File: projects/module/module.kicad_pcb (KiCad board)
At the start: 2 copper layers, 21 x 51 mm, 18 parts, among them J1 Conn_01x08_Pin, Y1 Crystal_GND24

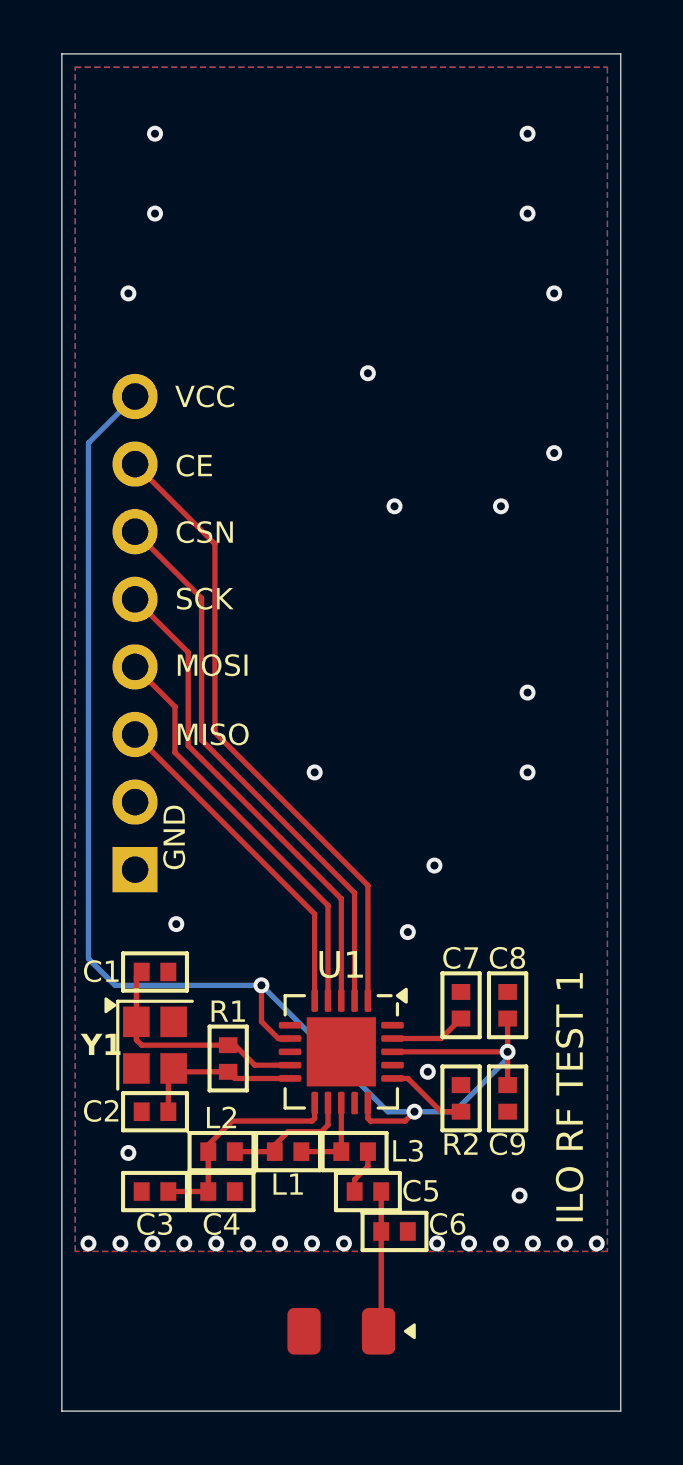
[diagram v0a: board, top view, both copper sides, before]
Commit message: Added breakout module. Added custom thin header holes. Sunk USB-C
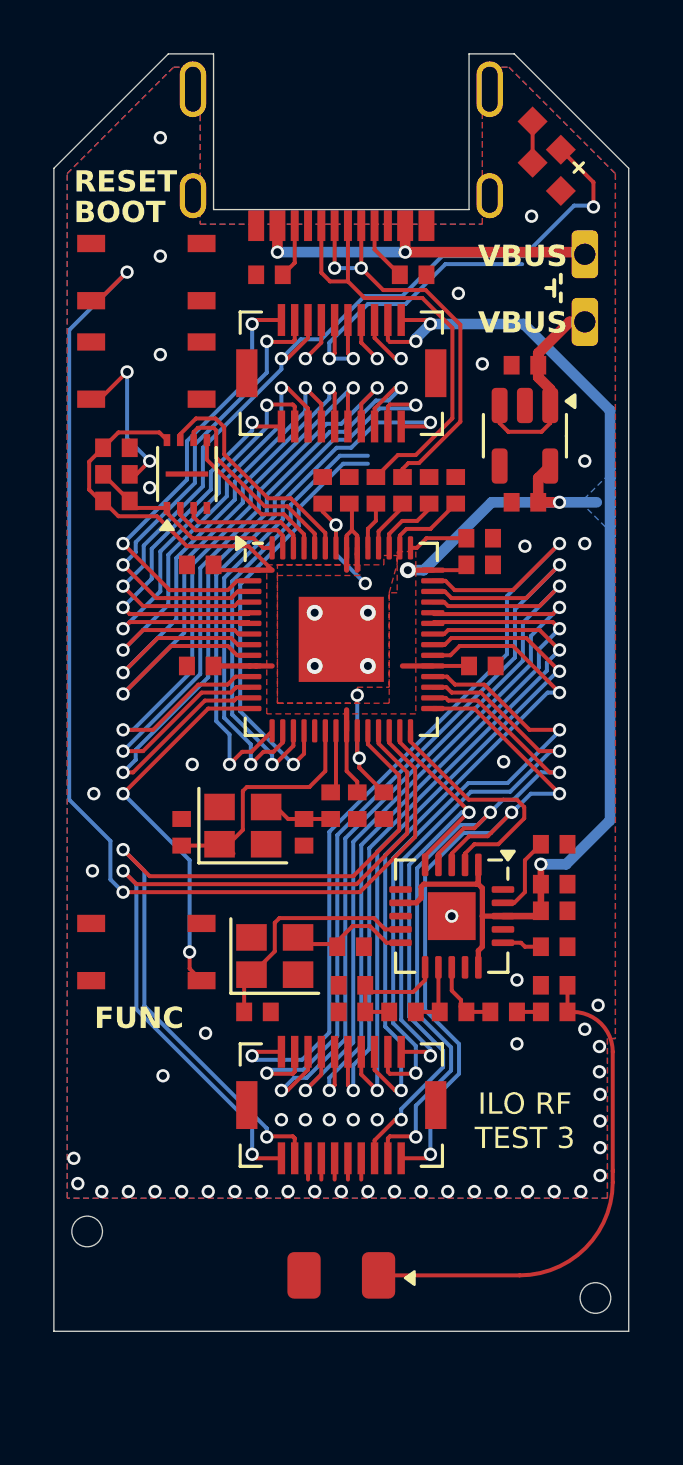
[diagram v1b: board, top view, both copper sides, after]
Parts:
- removed R1: 1M, ILO_fp:0402
- added C1: 1uF, ILO_fp:0402_compact, F.Cu at (46.9, 41.7)
- added C10: 1uF, ILO_fp:0402_compact, F.Cu at (44.3, 46.4)
- added C11: 100nF, ILO_fp:0402_compact, F.Cu at (34.7, 49.2)
- added C12: 100nF, ILO_fp:0402_compact, F.Cu at (45.3, 53.0)
- added C13: 100nF, ILO_fp:0402_compact, F.Cu at (34.7, 53.0)
- added C14: 100nF, ILO_fp:0402_compact, F.Cu at (40.6, 58.2)
- added C15: 100nF, ILO_fp:0402_compact, F.Cu at (45.2, 49.2)
- added C16: 100nF, ILO_fp:0402_compact, F.Cu at (45.2, 48.2)
- added C2: 15pF, ILO_fp:0402_compact, F.Cu at (34.0, 59.2)
- added C20: 100nF, ILO_fp:0402_compact, F.Cu at (31.6, 44.8)
- added C3: 15pF, ILO_fp:0402_compact, F.Cu at (38.6, 59.2)
- added C4: 1uF, ILO_fp:0402_compact, F.Cu at (46.9, 46.9)
- added C6: 100nF, ILO_fp:0402_compact, F.Cu at (39.3, 46.4)
- added C7: 100nF, ILO_fp:0402_compact, F.Cu at (41.6, 58.2)
- added C8: 1uF, ILO_fp:0402_compact, F.Cu at (43.3, 46.4)
- added C9: 100nF, ILO_fp:0402_compact, F.Cu at (40.3, 46.4)
- added D1: Diode, ILO_fp:0603_d, F.Cu at (47.7, 33.1)
- added J2: Conn_01x20_Pin, ILO_fp:Hirose_DF12NB, F.Cu at (40.0, 42.0)
- added J3: Conn_01x20_Pin, ILO_fp:Hirose_DF12NB, F.Cu at (40.0, 69.5)
- added R20: 1KΩ, ILO_fp:0402_compact, F.Cu at (31.6, 45.8)
- added R21: 10KΩ, ILO_fp:0402_compact, F.Cu at (31.6, 46.8)
- added R3: 27Ω, ILO_fp:0402_compact, F.Cu at (41.3, 46.4)
- added R4: 27Ω, ILO_fp:0402_compact, F.Cu at (42.3, 46.4)
- added R5: 1KΩ, ILO_fp:0402_compact, F.Cu at (39.6, 58.2)
- added R50: 5.1KΩ, ILO_fp:0402_compact, F.Cu at (42.7, 38.3)
- added R51: 5.1KΩ, ILO_fp:0402_compact, F.Cu at (37.3, 38.3)
- added R6: 20Ω, ILO_fp:0603, F.Cu at (47.7, 34.6)
- added REF**: SMT, ILO_fp:JLCPCB_SMT_hole, F.Cu at (49.5, 76.8)
- added REF**: SMT, ILO_fp:JLCPCB_SMT_hole, F.Cu at (30.4, 74.2)
- added SW1: SW_Push, ILO_fp:Alpsalpine_SKRP_compact, F.Cu at (32.7, 41.9)
- added SW2: SW_Push, ILO_fp:Alpsalpine_SKRP_compact, F.Cu at (32.7, 38.2)
- added SW3: SW_Push, ILO_fp:Alpsalpine_SKRP_compact, F.Cu at (32.7, 63.8)
- added SW4: SW_Push, ILO_fp:Header_2x_compact, F.Cu at (49.1, 37.5)
- added U2: FLASH, ILO_fp:Winbond_W25Q, F.Cu at (34.2, 45.8)
- added U4: NRF24, ILO_fp:QFN20_internal_routing, F.Cu at (44.1, 62.4)
- added U5: LDK130, Package_TO_SOT_SMD:SOT-23-5, F.Cu at (46.9, 44.4)
- added Y1: 12MHz, Crystal:Crystal_SMD_2520-4Pin_2.5x2.0mm, F.Cu at (36.3, 59.0)
- C40: renamed from C9; footprint ILO_fp:0402 -> ILO_fp:0402_compact
- C41: renamed from C8; footprint ILO_fp:0402 -> ILO_fp:0402_compact
- C42: renamed from C7; footprint ILO_fp:0402 -> ILO_fp:0402_compact
- C43: renamed from C1; footprint ILO_fp:0402 -> ILO_fp:0402_compact
- C44: renamed from C2; footprint ILO_fp:0402 -> ILO_fp:0402_compact
- C45: renamed from C3; footprint ILO_fp:0402 -> ILO_fp:0402_compact
- C46: renamed from C4; footprint ILO_fp:0402 -> ILO_fp:0402_compact
- C47: renamed from C5; footprint ILO_fp:0402 -> ILO_fp:0402_compact
- C48: renamed from C6; value 1.0pF -> 1pF; footprint ILO_fp:0402 -> ILO_fp:0402_compact
- J1: value Conn_01x08_Pin -> USB_C; footprint Connector_PinHeader_2.54mm:PinHeader_1x08_P2.54mm_Vertical -> ILO_fp:USB_C2927298
- L1, L2, L3: footprint ILO_fp:0402 -> ILO_fp:0402_compact
- R40: renamed from R2; value 22K -> 22KΩ; footprint ILO_fp:0402 -> ILO_fp:0402_compact
- U1: value ~ -> RP2040; footprint Package_DFN_QFN:QFN-20-1EP_4x4mm_P0.5mm_EP2.6x2.6mm -> Package_DFN_QFN:QFN-56-1EP_7x7mm_P0.4mm_EP3.2x3.2mm
- Y2: renamed from Y1; value Crystal_GND24 -> 16MHz
- moved U1 15.5 mm to (40.0, 52.0), turned to 0 degrees
- moved J1 11.9 mm to (40.0, 33.9), turned to 180 degrees
- moved C48 11.0 mm to (48.0, 65.0), turned to 180 degrees
- moved C45 10.0 mm to (40.4, 66.0)
- moved C47 9.72 mm to (48.0, 66.0)
- moved C44 9.62 mm to (40.4, 63.5), turned to 0 degrees
- moved C46 9.17 mm to (40.4, 65.0), turned to 180 degrees
- moved L2 8.59 mm to (42.3, 66.0)
- moved C40 8.24 mm to (48.0, 61.2), turned to 0 degrees
- moved L1 8.12 mm to (44.2, 66.0)
- moved L3 7.68 mm to (46.1, 66.0)
- moved C42 6.99 mm to (48.0, 59.7), turned to 0 degrees
- moved R40 6.69 mm to (48.0, 63.5), turned to 180 degrees
- moved Y2 5.61 mm to (37.5, 63.9), turned to 0 degrees
- moved C43 4.13 mm to (36.9, 66.0)
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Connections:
- C40 pad 1: VCC -> +3V3
- C41 pad 1: VCC -> +3V3
- C42 pad 1: GND -> Net-(U4-DVDD)
- C42 pad 2: Net-(U1-DVDD) -> GND
- C43 pad 1: Net-(U1-XC2) -> Net-(U4-XC2)
- C44 pad 1: Net-(U1-XC1) -> Net-(U4-XC1)
- C45 pad 1: Net-(U1-VDDPA) -> Net-(U4-VDDPA)
- C46 pad 1: Net-(U1-VDDPA) -> Net-(U4-VDDPA)
- L1 pad 1: Net-(U1-ANT2) -> Net-(U4-ANT2)
- L1 pad 2: Net-(U1-ANT1) -> Net-(U4-ANT1)
- L2 pad 1: Net-(U1-ANT1) -> Net-(U4-ANT1)
- L2 pad 2: Net-(U1-VDDPA) -> Net-(U4-VDDPA)
- L3 pad 1: Net-(U1-ANT2) -> Net-(U4-ANT2)
- R40 pad 2: Net-(U1-IREF) -> Net-(U4-IREF)
- U1 pad 1: CE -> +3V3
- U1 pad 10: Net-(U1-XC1) -> +3V3
- U1 pad 11: Net-(U1-VDDPA) -> /GP8
- U1 pad 12: Net-(U1-ANT1) -> /GP9
- U1 pad 13: Net-(U1-ANT2) -> /GP10
- U1 pad 14: GND -> /GP11
- U1 pad 15: VCC -> /GP12
- U1 pad 16: Net-(U1-IREF) -> /GP13
- U1 pad 17: GND -> /GP14
- U1 pad 18: VCC -> /GP15
- U1 pad 19: Net-(U1-DVDD) -> GND
- U1 pad 2: CSN -> /UART_TX
- U1 pad 20: GND -> /XIN
- U1 pad 21: (no net) -> /XOUT
- U1 pad 3: SCK -> /UART_RX
- U1 pad 4: MOSI -> /GP2
- U1 pad 5: MISO -> /GP3
- U1 pad 6: unconnected-(U1-IRQ-Pad6) -> /GP4
- U1 pad 7: VCC -> /GP5
- U1 pad 8: GND -> /GP6
- U1 pad 9: Net-(U1-XC2) -> /GP7
- Y2 pad 1: Net-(U1-XC2) -> Net-(U4-XC2)
- Y2 pad 3: Net-(U1-XC1) -> Net-(U4-XC1)
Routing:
- net +3V3: track 0.00 -> 88.3 mm, vias 0 -> 5
- net VCC: track 53.1 -> 0.00 mm, vias 3 -> 0
- net Net-(U1-RUN): track 0.00 -> 43.1 mm, vias 0 -> 2
- net /GP2: track 0.00 -> 34.9 mm, vias 0 -> 3
- net /ADC3: track 0.00 -> 32.1 mm, vias 0 -> 2
- net /ADC2: track 0.00 -> 31.7 mm, vias 0 -> 2
- net /ADC1: track 0.00 -> 30.8 mm, vias 0 -> 2
- net /SWCLK: track 0.00 -> 30.6 mm, vias 0 -> 2
- net /SWDIO: track 0.00 -> 29.8 mm, vias 0 -> 2
- net /SPI_TX: track 0.00 -> 29.0 mm, vias 0 -> 3
- net /ADC0: track 0.00 -> 28.7 mm, vias 0 -> 2
- net /SPI_CLK: track 0.00 -> 28.6 mm, vias 0 -> 3
- net /GP25: track 0.00 -> 27.4 mm, vias 0 -> 2
- net /GP10: track 0.00 -> 27.3 mm, vias 0 -> 2
- net /GP24: track 0.00 -> 26.6 mm, vias 0 -> 2
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- added copper zone on F.Cu, net +1V1
- added copper zone on B.Cu, net +3V3
- added copper zone on F.Cu, net +3V3
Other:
- board size 21 x 51 mm -> 21.6 x 48 mm
- board text added: "BOOT"
- board text added: "FUNC"
- board text added: "ILO RF TEST 3"
- board text added: "JLCJLCJLCJLC"
- board text added: "RESET"
- board text added: "VBUS"
- board text added: "x"
- board text removed: "CE"
- board text removed: "CSN"
- board text removed: "GND"
- board text removed: "ILO RF TEST 1"
- board text removed: "MISO"
- board text removed: "MOSI"
- board text removed: "SCK"
- board text removed: "VCC"

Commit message: RF module test 4
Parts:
- removed SW2, SW3: SW_Push, ILO_fp:Alpsalpine_SKRP_compact
- removed SW4: SW_Push, ILO_fp:Header_2x_compact
- added C30: 10uF, ILO_fp:0402_compact, F.Cu at (47.0, 35.1)
- added C32: 4.7uF, ILO_fp:0402_compact, F.Cu at (48.0, 35.1)
- added J4: Conn_01x01_Pin, ILO_fp:Pad_1mm, F.Cu at (44.3, 37.8)
- added J5: Conn_01x01_Pin, ILO_fp:Pad_1mm, F.Cu at (45.0, 44.7)
- added R32: 3.3KΩ, ILO_fp:0402_compact, F.Cu at (49.0, 35.1)
- added R33: 10KΩ, ILO_fp:0402_compact, F.Cu at (48.8, 42.4)
- added R34: 10KΩ, ILO_fp:0402_compact, F.Cu at (45.5, 42.9)
- added U3: MCP73871, ILO_fp:QFN20_internal_routing, F.Cu at (47.3, 39.3)
- J1: footprint ILO_fp:USB_C2927298 -> ILO_fp:USB_C3019717
- moved D1 15.4 mm to (32.3, 33.1), turned to -135 degrees
- moved R6 15.4 mm to (32.3, 34.6), turned to 45 degrees
- moved C51 11.3 mm to (47.9, 63.4), turned to 90 degrees
- moved C57 10.3 mm to (48.0, 70.0)
- moved C56 10.3 mm to (40.5, 72.0), turned to 0 degrees
- moved C59 9.98 mm to (48.0, 71.2), turned to 180 degrees
- moved C55 9.20 mm to (40.0, 70.5), turned to -90 degrees
- moved C58 9.16 mm to (46.1, 71.2)
- moved R52 9.09 mm to (43.0, 71.2), turned to 0 degrees
- moved Y2 8.37 mm to (45.9, 63.4), turned to 90 degrees
- moved J3 7.50 mm to (40.0, 62.0)
- moved L3 6.65 mm to (40.0, 68.7), turned to -90 degrees
- moved C52 5.70 mm to (45.5, 61.1)
- moved U5 5.56 mm to (44.3, 68.0), turned to 90 degrees
- moved C3 4.83 mm to (34.5, 61.8), turned to 180 degrees
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- renumbered C1 to C41, C4 to C42, C43 to C51, C44 to C52, C45 to C53, C46 to C54, C47 to C55, C48 to C56, C42 to C57, C41 to C58, C40 to C59, R40 to R52, U5 to U4, U4 to U5
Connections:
- net Net-(U5-EN) renamed VSYS
- D1 pad 2: /GP2 -> /GP3
- J2 pad 11: /GP3 -> /GP4
- J2 pad 12: /GP4 -> /GP5
- J2 pad 13: /GP5 -> /GP6
- J2 pad 14: /GP6 -> /GP7
- J2 pad 15: /GP7 -> /GP8
- J2 pad 16: /GP8 -> /GP9
- J2 pad 17: /GP9 -> /GP10
- J2 pad 18: /GP10 -> /GP11
- J2 pad 3: /GP2 -> GND
- J2 pad 4: unconnected-(J2-Pin_4-Pad4) -> GND
- J3 pad 11: /SWDIO -> GND
- J3 pad 12: /SWCLK -> GND
- J3 pad 17: GND -> /RUN
- R20 pad 1: Net-(R20-Pad1) -> /GP2
- SW1 pad 2: Net-(R20-Pad1) -> /GP2
- U1 pad 26: Net-(U1-RUN) -> /RUN
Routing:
- net Net-(U1-RUN): track 43.1 -> 0.00 mm, vias 2 -> 0
- net /SWCLK: track 30.6 -> 0.00 mm, vias 2 -> 0
- net /SWDIO: track 29.8 -> 0.00 mm, vias 2 -> 0
- net Net-(AE1-A): track 19.6 -> 3.80 mm
- net /GP2: track 34.9 -> 19.8 mm
- net /GP11: track 14.4 -> 28.3 mm
- net +3V3: track 88.3 -> 101.9 mm
- net /RUN: track 0.00 -> 11.9 mm, vias 0 -> 2
- net /GP17: track 9.69 -> 19.0 mm
- net /GP15: track 16.1 -> 25.2 mm, vias 1 -> 2
- net /I2C_SDA: track 22.4 -> 13.7 mm
- net /GP3: track 15.0 -> 23.7 mm
- net /I2C_SCL: track 24.2 -> 15.7 mm
- net /GP14: track 16.6 -> 25.1 mm, vias 1 -> 2
- net /GP22: track 25.9 -> 17.6 mm
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- added copper zone on F.Cu, net VSYS
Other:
- board size 21.6 x 48 mm -> 21.6 x 48.5 mm
- board text added: "BOOT+"
- board text added: "ILO RF TEST 4"
- board text removed: "BOOT"
- board text removed: "FUNC"
- board text removed: "ILO RF TEST 3"
- board text removed: "RESET"
- board text removed: "VBUS"
- board text removed: "x"

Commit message: RF module test 5
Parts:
- removed J4, J5: Conn_01x01_Pin, ILO_fp:Pad_1mm
- removed the REF** at (49.5, 77.2)
- removed the REF** at (30.5, 73.8)
- added REF**: Pad_1mm, ILO_fp:Pad_1mm, B.Cu at (63.0, 47.5)
- added REF**: Pad_1mm, ILO_fp:Pad_1mm, B.Cu at (69.0, 35.0)
- added REF**: Pad_1mm, ILO_fp:Pad_1mm, B.Cu at (64.2, 45.5)
- added REF**: Pad_1mm, ILO_fp:Pad_1mm, B.Cu at (69.0, 37.6)
- added REF**: Pad_1mm, ILO_fp:Pad_1mm, B.Cu at (66.5, 41.1)
- added REF**: Pad_1mm, ILO_fp:Pad_1mm, B.Cu at (67.4, 35.0)
- added REF**: Pad_1mm, ILO_fp:Pad_1mm, B.Cu at (68.2, 41.1)
- moved C56 21.5 mm to (61.9, 73.5)
- moved C55 21.0 mm to (60.9, 72.3), turned to 0 degrees
- moved R52 20.7 mm to (63.6, 69.5), turned to 90 degrees
- moved L3 20.6 mm to (60.4, 71.2), turned to 0 degrees
- moved AE1 20.0 mm to (60.0, 77.0), turned to 180 degrees
- moved C41 20.0 mm to (66.9, 43.4)
- moved U3 20.0 mm to (67.3, 39.3)
- moved C10 20.0 mm to (64.3, 46.4)
- moved C11 20.0 mm to (54.7, 49.2)
- moved C12 20.0 mm to (65.3, 53.0)
- moved C13 20.0 mm to (54.7, 53.0)
- moved C14 20.0 mm to (60.2, 58.1)
- moved C15 20.0 mm to (65.2, 49.2)
- moved C16 20.0 mm to (65.2, 48.2)
- moved C2 20.0 mm to (52.2, 59.6)
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- renumbered R50 to R40, R51 to R41
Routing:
- net /SPI_CLK: track 27.1 -> 20.2 mm
- net /SPI_TX: track 27.4 -> 21.2 mm
- net /SPI_RX: track 23.2 -> 18.1 mm, vias 2 -> 3
- net +3V3: track 101.9 -> 99.7 mm
- net Net-(U5-ANT1): track 2.48 -> 4.46 mm
- net Net-(U5-XC2): track 5.21 -> 7.19 mm
- net VBUS: track 15.8 -> 17.8 mm, vias 2 -> 3
- net /BAT+: track 17.6 -> 19.5 mm
- net Net-(U3-PROG3): track 3.40 -> 5.05 mm, vias 0 -> 1
- net Net-(U5-DVDD): track 3.53 -> 1.91 mm
- net GND: track 14.5 -> 13.1 mm, vias 61 -> 52
- net Net-(U3-PROG1): track 4.46 -> 5.71 mm, vias 0 -> 1
- net /GP17: track 19.0 -> 17.9 mm, vias 0 -> 2
- net Net-(U5-VDDPA): track 6.44 -> 7.37 mm
- net VSYS: track 13.2 -> 14.1 mm, vias 0 -> 1
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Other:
- board size 21.6 x 48.5 mm -> 70 x 70 mm
- board text added: "BAT"
- board text added: "EDGE RAIL V-CUT"
- board text added: "GND"
- board text added: "ILO RF TEST 5"
- board text added: "P1"
- board text added: "P3"
- board text added: "TH"
- board text added: "VB"
- board text added: "VSYS"
- board text removed: "ILO RF TEST 4"

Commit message: RF module test 6
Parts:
- AE1: footprint Diode_SMD:D_1206_3216Metric -> ILO_fp:Yageo_ANT3216
- moved C52 14.1 mm to (65.8, 61.3), turned to 0 degrees
- moved C51 13.7 mm to (67.8, 64.2), turned to 90 degrees
- moved Y2 12.2 mm to (65.8, 63.5), turned to 90 degrees
- moved C53 9.18 mm to (60.6, 67.3), turned to 90 degrees
- moved C54 7.96 mm to (61.6, 67.3), turned to 90 degrees
- moved C57 6.95 mm to (69.2, 70.8), turned to -90 degrees
- moved L2 6.18 mm to (61.1, 68.8)
- moved U5 6.01 mm to (66.0, 68.0), turned to 90 degrees
- moved L1 5.02 mm to (62.5, 69.3), turned to 90 degrees
- moved C58 4.83 mm to (65.8, 71.3), turned to 180 degrees
- moved C59 3.31 mm to (67.7, 71.3), turned to 0 degrees
- moved R52 1.87 mm to (63.9, 71.3), turned to 180 degrees
- moved L3 1.48 mm to (61.5, 70.3), turned to -90 degrees
- moved C55 0.67 mm to (61.5, 72.2), turned to -90 degrees
- moved C56 0.20 mm to (62.0, 73.6)
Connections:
- net /I2C_SCL renamed /GP21
- net /I2C_SDA renamed /GP20
- U3 pad 11: unconnected-(U3-VSS-Pad11) -> GND
- U3 pad 15: unconnected-(U3-VBAT-Pad15) -> /BAT+
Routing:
- net /SPI_CLK: track 20.2 -> 26.5 mm
- net /SPI_TX: track 21.2 -> 26.6 mm
- net /SPI_RX: track 18.1 -> 21.9 mm, vias 3 -> 2
- net Net-(U5-XC2): track 7.19 -> 3.81 mm
- net Net-(U5-VDDPA): track 7.37 -> 4.90 mm
- net Net-(U5-DVDD): track 1.91 -> 3.30 mm
- net +3V3: track 99.7 -> 101.0 mm
- net Net-(U5-ANT1): track 4.46 -> 3.26 mm
- net Net-(U5-IREF): track 1.43 -> 2.58 mm
- net Net-(U5-ANT2): track 2.82 -> 3.78 mm
- net /GP17: track 17.9 -> 18.1 mm, vias 2 -> 0
- net GND: vias 52 -> 66
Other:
- board size 70 x 70 mm -> 21.6 x 48.5 mm
- board text added: "ILO RF TEST 6"
- board text removed: "ILO RF TEST 5"

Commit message: RF module test 7
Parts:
- moved C51 5.11 mm to (66.5, 59.2), turned to 180 degrees
- moved C56 4.08 mm to (60.5, 69.8)
- moved C55 3.49 mm to (60.5, 68.8), turned to 180 degrees
- moved R52 3.27 mm to (65.0, 68.2), turned to 0 degrees
- moved AE1 3.05 mm to (60.0, 74.0), turned to -90 degrees
- moved U5 2.93 mm to (66.7, 65.2)
- moved L1 2.70 mm to (63.1, 66.7), turned to 135 degrees
- moved C57 2.69 mm to (68.5, 68.2), turned to 0 degrees
- moved Y2 2.64 mm to (67.1, 61.2), turned to 180 degrees
- moved L3 2.41 mm to (62.4, 68.0), turned to -135 degrees
- moved C59 2.10 mm to (67.6, 69.2)
- moved C58 2.10 mm to (65.7, 69.2)
- moved L2 1.60 mm to (61.7, 67.3), turned to -135 degrees
- moved C54 1.51 mm to (61.0, 65.9), turned to 135 degrees
- moved C52 0.89 mm to (65.0, 61.6), turned to 90 degrees
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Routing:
- net Net-(AE1-A): track 4.42 -> 1.00 mm
- net Net-(U5-XC1): track 5.44 -> 2.91 mm
- net +3V3: track 101.0 -> 98.5 mm
- net /SPI_CLK: track 26.5 -> 28.4 mm
- net Net-(U5-DVDD): track 3.30 -> 1.49 mm
- net Net-(U5-XC2): track 3.81 -> 5.56 mm
- net /GP20: track 13.7 -> 15.1 mm
- net Net-(U5-IREF): track 2.58 -> 1.19 mm
- net Net-(U5-VDDPA): track 4.90 -> 6.21 mm
- net /SPI_RX: track 21.9 -> 20.6 mm
- net /GP17: track 18.1 -> 17.3 mm
- net GND: vias 66 -> 60
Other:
- board size 21.6 x 48.5 mm -> 21.6 x 50.5 mm
- board text added: "ILO RF TEST 7"
- board text removed: "ILO RF TEST 6"

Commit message: RF module test 7.5
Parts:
- removed AE1: Antenna, ILO_fp:Yageo_ANT3216
- removed C51, C52: 22pF, ILO_fp:0402_compact
- removed C53: 2.2pF, ILO_fp:0402_compact
- removed C54: 4.7pF, ILO_fp:0402_compact
- removed C55: 1.5pF, ILO_fp:0402_compact
- removed C56: 1pF, ILO_fp:0402_compact
- removed C57: 33nF, ILO_fp:0402_compact
- removed C58: 1nF, ILO_fp:0402_compact
- removed C59: 10nF, ILO_fp:0402_compact
- removed L1: 8.2nH, ILO_fp:0402_compact
- removed L2: 2.7nH, ILO_fp:0402_compact
- removed L3: 3.9nH, ILO_fp:0402_compact
- removed R52: 22KΩ, ILO_fp:0402_compact
- removed U5: NRF24, ILO_fp:QFN20_internal_routing
- removed Y2: 16MHz, Crystal:Crystal_SMD_2520-4Pin_2.5x2.0mm
- added ?: , clipboard:5e7cfdf6-62b4-49b8-8e4d-08e3e4b200c4, F.Cu at (67.1, 74.6)
- added REF**: Espressif_ESP32_mini, ILO_fp:Espressif_ESP32_mini, F.Cu at (60.0, 70.5)
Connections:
- net /GP20 renamed /UART1_TX
- net /GP21 renamed /UART1_RX
- net /GP22 renamed /I2C_SDA
- net /GP23 renamed /I2C_SCL
- net /UART_RX renamed /UART0_RX
- net /UART_TX renamed /UART0_TX
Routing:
- net /UART1_RX: track 15.9 -> 40.0 mm, vias 2 -> 3
- net /UART1_TX: track 15.1 -> 36.7 mm, vias 2 -> 3
- net /GP24: track 19.1 -> 38.2 mm, vias 2 -> 3
- net /SPI_CLK: track 28.4 -> 15.7 mm, vias 3 -> 2
- net /SPI_TX: track 27.1 -> 16.2 mm, vias 3 -> 2
- net /SPI_RX: track 20.6 -> 11.4 mm
- net +3V3: track 98.5 -> 90.9 mm
- net Net-(U5-VDDPA): track 6.21 -> 0.00 mm
- net Net-(U5-XC2): track 5.56 -> 0.00 mm
- net /GP17: track 17.3 -> 22.1 mm, vias 0 -> 2
- net Net-(U5-ANT1): track 3.69 -> 0.00 mm
- net Net-(U5-ANT2): track 3.57 -> 0.00 mm
- net Net-(U5-XC1): track 2.91 -> 0.00 mm
- net Net-(U5-DVDD): track 1.49 -> 0.00 mm
- net Net-(C55-Pad1): track 1.27 -> 0.00 mm
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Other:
- board size 21.6 x 50.5 mm -> 21.6 x 46.1 mm
- board text added: "ILO RF TEST"
- board text removed: "ILO RF TEST 7"

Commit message: RF module test 8
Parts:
- removed the REF** at (60.0, 70.5)
- added C50: 100nF, ILO_fp:0402_compact, F.Cu at (68.8, 71.8)
- added C51: 10uF, ILO_fp:0402_compact, F.Cu at (68.8, 72.8)
- added C52: 1uF, ILO_fp:0402_compact, F.Cu at (68.8, 67.8)
- added C61: 100nF, ILO_fp:0402_compact, F.Cu at (68.8, 51.5)
- added C62: 100nF, ILO_fp:0402_compact, F.Cu at (68.8, 50.5)
- added C63: 100nF, ILO_fp:0402_compact, F.Cu at (68.8, 49.5)
- added C64: 100nF, ILO_fp:0402_compact, F.Cu at (68.8, 48.5)
- added R50: 10KΩ, ILO_fp:0402_compact, F.Cu at (68.8, 68.9)
- added SW2: SW_Push, ILO_fp:Alpsalpine_SKRP_compact, F.Cu at (67.2, 62.0)
- added U5: ESP32, ILO_fp:Espressif_ESP32_mini, F.Cu at (60.0, 70.5)
- moved C15 0.07 mm to (65.2, 49.1)
- moved C16 0.07 mm to (65.2, 48.1)
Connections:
- J2 pad 3: GND -> unconnected-(J2-Pin_3-Pad3)
- J2 pad 4: GND -> unconnected-(J2-Pin_4-Pad4)
- J3 pad 13: GND -> unconnected-(J3-Pin_13-Pad13)
- J3 pad 14: GND -> unconnected-(J3-Pin_14-Pad14)
- J3 pad 15: GND -> unconnected-(J3-Pin_15-Pad15)
- J3 pad 16: GND -> unconnected-(J3-Pin_16-Pad16)
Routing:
- net /GP24: track 38.2 -> 17.8 mm, vias 3 -> 2
- net /GP25: track 19.9 -> 39.1 mm, vias 2 -> 3
- net GND: track 13.1 -> 17.9 mm, vias 30 -> 27
- net Net-(U5-EN): track 0.00 -> 3.50 mm
- net /GP17: track 22.1 -> 25.5 mm
- net +3V3: track 90.9 -> 94.2 mm
- net unconnected-(J2-Pin_3-Pad3): track 0.00 -> 2.00 mm, vias 0 -> 1
- net unconnected-(J2-Pin_4-Pad4): track 0.00 -> 1.70 mm, vias 0 -> 1
- net /UART1_RX: track 40.0 -> 41.2 mm
- net /UART1_TX: track 36.7 -> 37.8 mm
- net /I2C_SCL: track 18.2 -> 17.1 mm
- net /I2C_SDA: track 17.5 -> 16.6 mm
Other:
- board size 21.6 x 46.1 mm -> 70 x 70 mm
- board text added: "ILO RF TEST 8"
- board text removed: "ILO RF TEST"
- board text removed: "JLCJLCJLCJLC"
